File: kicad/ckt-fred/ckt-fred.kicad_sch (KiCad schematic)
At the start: 20 parts, among them J2 AVR-ISP, U1 AP7381-33Y

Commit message: Start of FRED PCB
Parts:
- BT1: renamed from BT?; footprint (none) -> Battery:BatteryHolder_Keystone_3034_1x20mm
- D5: renamed from D?; value CDBM140G -> BAT43W
- R1, R2: renamed from R?; footprint (none) -> Resistor_SMD:R_0805_2012Metric
- gave numbers to parts that had none: 5
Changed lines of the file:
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@@
   (symbol (lib_id "Device:R_US") (at 132.08 119.38 90) (unit 1)
     (in_bom yes) (on_board yes) (fields_autoplaced)
-    (property "Reference" "R?" (id 0) (at 132.08 113.03 90))
+    (property "Reference" "R2" (id 0) (at 132.08 113.03 90))
     (property "Value" "330" (id 1) (at 132.08 115.57 90))
-    (property "Footprint" "" (id 2) (at 132.334 118.364 90)
+    (property "Footprint" "Resistor_SMD:R_0805_2012Metric" (id 2) (at 132.334 118.364 90)
       (effects (font (size 1.27 1.27)) hide)
     )
@@
   (symbol (lib_id "MCU_Microchip_ATtiny:ATtiny13-20SS") (at 117.475 89.535 0) (mirror y) (unit 1)
     (in_bom yes) (on_board yes) (fields_autoplaced)
-    (property "Reference" "U?" (id 0) (at 131.445 88.2649 0)
-      (effects (font (size 1.27 1.27)) (justify right))
-    )
-    (property "Value" "ATtiny13-20SS" (id 1) (at 131.445 90.8049 0)
+    (property "Reference" "U3" (id 0) (at 132.08 88.2649 0)
+      (effects (font (size 1.27 1.27)) (justify right))
+    )
+    (property "Value" "ATtiny13-20SS" (id 1) (at 132.08 90.8049 0)
       (effects (font (size 1.27 1.27)) (justify right))
     )
@@
   (symbol (lib_id "power:GND") (at 144.78 125.095 0) (unit 1)
     (in_bom yes) (on_board yes)
-    (property "Reference" "#PWR?" (id 0) (at 144.78 131.445 0)
+    (property "Reference" "#PWR06" (id 0) (at 144.78 131.445 0)
       (effects (font (size 1.27 1.27)) hide)
     )
@@
   (symbol (lib_id "power:GND") (at 97.79 111.125 0) (unit 1)
     (in_bom yes) (on_board yes)
-    (property "Reference" "#PWR?" (id 0) (at 97.79 117.475 0)
+    (property "Reference" "#PWR02" (id 0) (at 97.79 117.475 0)
       (effects (font (size 1.27 1.27)) hide)
     )
@@
   (symbol (lib_id "Device:D_Schottky") (at 128.905 28.575 0) (mirror x) (unit 1)
     (in_bom yes) (on_board yes)
-    (property "Reference" "D?" (id 0) (at 132.08 31.115 0)
-      (effects (font (size 1.27 1.27)) (justify right))
-    )
-    (property "Value" "CDBM140G" (id 1) (at 127.635 31.115 0)
-      (effects (font (size 1.27 1.27)) (justify right) hide)
+    (property "Reference" "D5" (id 0) (at 132.08 31.115 0)
+      (effects (font (size 1.27 1.27)) (justify right))
+    )
+    (property "Value" "BAT43W" (id 1) (at 127.635 31.115 0)
+      (effects (font (size 1.27 1.27)) (justify right))
     )
     (property "Footprint" "ISE_Generic:SOD-123T" (id 2) (at 128.905 28.575 0)
@@
   (symbol (lib_id "Connector:TestPoint") (at 149.86 121.92 270) (mirror x) (unit 1)
     (in_bom yes) (on_board yes)
-    (property "Reference" "TP?" (id 0) (at 152.4 124.46 90)
+    (property "Reference" "TP3" (id 0) (at 152.4 124.46 90)
       (effects (font (size 1.27 1.27)) (justify right))
     )
@@
   (symbol (lib_id "Jumper:SolderJumper_2_Open") (at 97.79 107.315 90) (unit 1)
     (in_bom yes) (on_board yes)
-    (property "Reference" "JP?" (id 0) (at 95.25 107.315 0))
+    (property "Reference" "JP1" (id 0) (at 95.25 107.315 0))
     (property "Value" "SolderJumper_2_Open" (id 1) (at 95.25 107.315 0)
       (effects (font (size 1.27 1.27)) hide)
@@
   (symbol (lib_id "Device:R_US") (at 52.705 97.155 0) (unit 1)
     (in_bom yes) (on_board yes) (fields_autoplaced)
-    (property "Reference" "R?" (id 0) (at 54.61 95.8849 0)
+    (property "Reference" "R1" (id 0) (at 54.61 95.8849 0)
       (effects (font (size 1.27 1.27)) (justify left))
     )
@@
       (effects (font (size 1.27 1.27)) (justify left))
     )
-    (property "Footprint" "" (id 2) (at 53.721 97.409 90)
+    (property "Footprint" "Resistor_SMD:R_0805_2012Metric" (id 2) (at 53.721 97.409 90)
       (effects (font (size 1.27 1.27)) hide)
     )
@@
   (symbol (lib_id "Device:Battery_Cell") (at 137.795 36.83 0) (unit 1)
     (in_bom yes) (on_board yes) (fields_autoplaced)
-    (property "Reference" "BT?" (id 0) (at 140.97 33.5279 0)
+    (property "Reference" "BT1" (id 0) (at 140.97 33.5279 0)
       (effects (font (size 1.27 1.27)) (justify left))
     )
@@
       (effects (font (size 1.27 1.27)) (justify left))
     )
-    (property "Footprint" "" (id 2) (at 137.795 35.306 90)
+    (property "Footprint" "Battery:BatteryHolder_Keystone_3034_1x20mm" (id 2) (at 137.795 35.306 90)
       (effects (font (size 1.27 1.27)) hide)
     )
@@
   (symbol (lib_id "power:GND") (at 36.83 114.3 0) (unit 1)
     (in_bom yes) (on_board yes)
-    (property "Reference" "#PWR?" (id 0) (at 36.83 120.65 0)
+    (property "Reference" "#PWR03" (id 0) (at 36.83 120.65 0)
       (effects (font (size 1.27 1.27)) hide)
     )
@@
   (symbol (lib_id "Connector:TestPoint") (at 149.86 119.38 270) (mirror x) (unit 1)
     (in_bom yes) (on_board yes)
-    (property "Reference" "TP?" (id 0) (at 148.59 117.475 90)
+    (property "Reference" "TP4" (id 0) (at 148.59 117.475 90)
       (effects (font (size 1.27 1.27)) (justify left))
     )
@@
   (symbol (lib_id "power:+3.3V") (at 36.83 86.995 0) (unit 1)
     (in_bom yes) (on_board yes)
-    (property "Reference" "#PWR?" (id 0) (at 36.83 90.805 0)
+    (property "Reference" "#PWR01" (id 0) (at 36.83 90.805 0)
       (effects (font (size 1.27 1.27)) hide)
     )
@@
   (symbol (lib_id "Sensor_Magnetic:DRV5033AJxDBZ") (at 39.37 104.14 0) (unit 1)
     (in_bom yes) (on_board yes) (fields_autoplaced)
-    (property "Reference" "U?" (id 0) (at 33.02 102.8699 0)
+    (property "Reference" "U2" (id 0) (at 33.02 102.8699 0)
       (effects (font (size 1.27 1.27)) (justify right))
     )
@@
   )
   (symbol_instances
+    (path "/c35f82c3-3c27-45b4-98d2-54a981722db7"
+      (reference "#PWR01") (unit 1) (value "+3.3V") (footprint "")
+    )
+    (path "/42964190-2646-44c8-8c9c-8b8e84134411"
+      (reference "#PWR02") (unit 1) (value "GND") (footprint "")
+    )
+    (path "/b6f1eb09-ad2b-486b-b398-9172b42670fe"
+      (reference "#PWR03") (unit 1) (value "GND") (footprint "")
+    )
     (path "/ca6a6475-1ce9-4d3a-92ad-0b7481036c88"
       (reference "#PWR04") (unit 1) (value "+3.3V") (footprint "")
@@
       (reference "#PWR05") (unit 1) (value "GND") (footprint "")
     )
+    (path "/14cc276f-9bde-461b-a8e9-cda296e71d13"
+      (reference "#PWR06") (unit 1) (value "GND") (footprint "")
+    )
     (path "/2a960e4c-7bd7-45a1-abd2-4f9380b618df"
       (reference "#PWR0105") (unit 1) (value "GND") (footprint "")
@@
       (reference "#PWR0113") (unit 1) (value "GND") (footprint "")
     )
-    (path "/14cc276f-9bde-461b-a8e9-cda296e71d13"
-      (reference "#PWR?") (unit 1) (value "GND") (footprint "")
-    )
-    (path "/42964190-2646-44c8-8c9c-8b8e84134411"
-      (reference "#PWR?") (unit 1) (value "GND") (footprint "")
-    )
-    (path "/b6f1eb09-ad2b-486b-b398-9172b42670fe"
-      (reference "#PWR?") (unit 1) (value "GND") (footprint "")
-    )
-    (path "/c35f82c3-3c27-45b4-98d2-54a981722db7"
-      (reference "#PWR?") (unit 1) (value "+3.3V") (footprint "")
-    )
     (path "/9a1452f2-4147-4a0f-b89d-767540ba8421"
-      (reference "BT?") (unit 1) (value "Battery_Cell") (footprint "")
+      (reference "BT1") (unit 1) (value "Battery_Cell") (footprint "Battery:BatteryHolder_Keystone_3034_1x20mm")
     )
     (path "/469e5709-28b1-4cf7-9f12-16395fc286c3"
@@
     )
     (path "/42bb5574-8de7-4a27-a12d-7306121c342e"
-      (reference "D?") (unit 1) (value "CDBM140G") (footprint "ISE_Generic:SOD-123T")
+      (reference "D5") (unit 1) (value "BAT43W") (footprint "ISE_Generic:SOD-123T")
     )
     (path "/743fd467-fa48-43d2-bdb1-0e709d925207"
@@
     )
     (path "/63977e5d-25ea-40a1-a869-d864a691de83"
-      (reference "JP?") (unit 1) (value "SolderJumper_2_Open") (footprint "Jumper:SolderJumper-2_P1.3mm_Open_RoundedPad1.0x1.5mm")
+      (reference "JP1") (unit 1) (value "SolderJumper_2_Open") (footprint "Jumper:SolderJumper-2_P1.3mm_Open_RoundedPad1.0x1.5mm")
+    )
+    (path "/8219c475-d6a1-455a-8dd4-ef0923356e4f"
+      (reference "R1") (unit 1) (value "100k") (footprint "Resistor_SMD:R_0805_2012Metric")
     )
     (path "/0aee1d11-4153-4a66-aa82-53a758d11c70"
-      (reference "R?") (unit 1) (value "330") (footprint "")
-    )
-    (path "/8219c475-d6a1-455a-8dd4-ef0923356e4f"
-      (reference "R?") (unit 1) (value "100k") (footprint "")
+      (reference "R2") (unit 1) (value "330") (footprint "Resistor_SMD:R_0805_2012Metric")
     )
     (path "/3d36f4c8-bdba-4d9c-8bb5-9b4a29689543"
@@
     )
     (path "/611c3ee3-155a-43e9-93d8-4698eb221164"
-      (reference "TP?") (unit 1) (value "TestPoint") (footprint "TestPoint:TestPoint_Pad_D2.0mm")
+      (reference "TP3") (unit 1) (value "TestPoint") (footprint "TestPoint:TestPoint_Pad_D2.0mm")
     )
     (path "/be05cc19-b0f7-4496-b019-4138adf19a10"
-      (reference "TP?") (unit 1) (value "TestPoint") (footprint "TestPoint:TestPoint_Pad_D2.0mm")
+      (reference "TP4") (unit 1) (value "TestPoint") (footprint "TestPoint:TestPoint_Pad_D2.0mm")
     )
     (path "/7a02355a-c87d-4d7e-9caa-076f50357812"
       (reference "U1") (unit 1) (value "AP7381-33Y") (footprint "ISE_Generic:SOT-89-3")
     )
+    (path "/d6778ce1-2501-4a7c-a126-0ea376c756f4"
+      (reference "U2") (unit 1) (value "DRV5032") (footprint "Package_TO_SOT_SMD:SOT-23")
+    )
     (path "/0cc7314a-3dbf-4203-939f-6c8913def138"
-      (reference "U?") (unit 1) (value "ATtiny13-20SS") (footprint "Package_SO:SOIC-8_3.9x4.9mm_P1.27mm")
-    )
-    (path "/d6778ce1-2501-4a7c-a126-0ea376c756f4"
-      (reference "U?") (unit 1) (value "DRV5032") (footprint "Package_TO_SOT_SMD:SOT-23")
-    )
-  )
+      (reference "U3") (unit 1) (value "ATtiny13-20SS") (footprint "Package_SO:SOIC-8_3.9x4.9mm_P1.27mm")
+    )
+  )

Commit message: A few updates
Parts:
- TP1, TP2, TP3, TP4: footprint TestPoint:TestPoint_Pad_D2.0mm -> TestPoint:TestPoint_Pad_4.0x4.0mm
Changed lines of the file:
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@@
       (effects (font (size 1.27 1.27)) (justify left) hide)
     )
-    (property "Footprint" "TestPoint:TestPoint_Pad_D2.0mm" (id 2) (at 29.21 23.495 0)
+    (property "Footprint" "TestPoint:TestPoint_Pad_4.0x4.0mm" (id 2) (at 29.21 23.495 0)
       (effects (font (size 1.27 1.27)) hide)
     )
@@
       (effects (font (size 1.27 1.27)) (justify left) hide)
     )
-    (property "Footprint" "TestPoint:TestPoint_Pad_D2.0mm" (id 2) (at 149.86 116.84 0)
+    (property "Footprint" "TestPoint:TestPoint_Pad_4.0x4.0mm" (id 2) (at 149.86 116.84 0)
       (effects (font (size 1.27 1.27)) hide)
     )
@@
       (effects (font (size 1.27 1.27)) (justify left) hide)
     )
-    (property "Footprint" "TestPoint:TestPoint_Pad_D2.0mm" (id 2) (at 29.21 26.035 0)
+    (property "Footprint" "TestPoint:TestPoint_Pad_4.0x4.0mm" (id 2) (at 29.21 26.035 0)
       (effects (font (size 1.27 1.27)) hide)
     )
@@
       (effects (font (size 1.27 1.27)) (justify left) hide)
     )
-    (property "Footprint" "TestPoint:TestPoint_Pad_D2.0mm" (id 2) (at 149.86 114.3 0)
+    (property "Footprint" "TestPoint:TestPoint_Pad_4.0x4.0mm" (id 2) (at 149.86 114.3 0)
       (effects (font (size 1.27 1.27)) hide)
     )
@@
     )
     (path "/3d36f4c8-bdba-4d9c-8bb5-9b4a29689543"
-      (reference "TP1") (unit 1) (value "TestPoint") (footprint "TestPoint:TestPoint_Pad_D2.0mm")
+      (reference "TP1") (unit 1) (value "TestPoint") (footprint "TestPoint:TestPoint_Pad_4.0x4.0mm")
     )
     (path "/6e81bcf9-ab29-4e46-90b9-1f0815b829a0"
-      (reference "TP2") (unit 1) (value "TestPoint") (footprint "TestPoint:TestPoint_Pad_D2.0mm")
+      (reference "TP2") (unit 1) (value "TestPoint") (footprint "TestPoint:TestPoint_Pad_4.0x4.0mm")
     )
     (path "/611c3ee3-155a-43e9-93d8-4698eb221164"
-      (reference "TP3") (unit 1) (value "TestPoint") (footprint "TestPoint:TestPoint_Pad_D2.0mm")
+      (reference "TP3") (unit 1) (value "TestPoint") (footprint "TestPoint:TestPoint_Pad_4.0x4.0mm")
     )
     (path "/be05cc19-b0f7-4496-b019-4138adf19a10"
-      (reference "TP4") (unit 1) (value "TestPoint") (footprint "TestPoint:TestPoint_Pad_D2.0mm")
+      (reference "TP4") (unit 1) (value "TestPoint") (footprint "TestPoint:TestPoint_Pad_4.0x4.0mm")
     )
     (path "/7a02355a-c87d-4d7e-9caa-076f50357812"

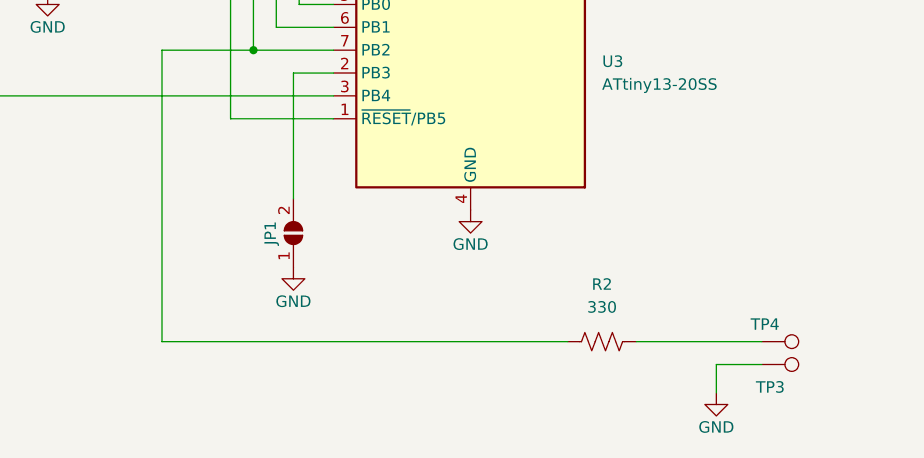
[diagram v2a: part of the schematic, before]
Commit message: Add output jumper to bypass resistor
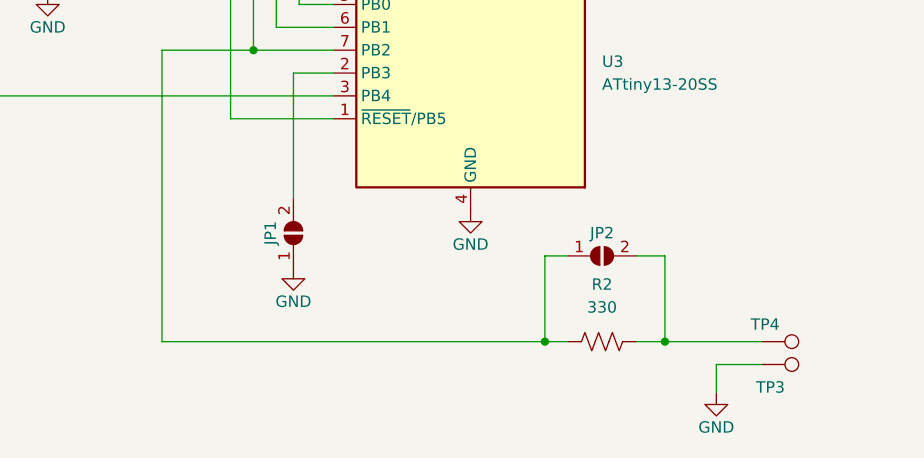
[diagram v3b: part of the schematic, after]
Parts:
- added JP2: SolderJumper_2_Open, Jumper:SolderJumper-2_P1.3mm_Open_RoundedPad1.0x1.5mm, symbol Jumper:SolderJumper_2_Open
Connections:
- net at J2.3 (SCK), R2.1, U3.7 (PB2): now also JP2.1 (A)
- net at R2.2, TP4.1: now also JP2.2 (B)
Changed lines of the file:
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@@
   (junction (at 69.215 46.355) (diameter 0) (color 0 0 0 0)
   )
+  (junction (at 139.065 119.38) (diameter 0) (color 0 0 0 0)
+  )
   (junction (at 118.11 28.575) (diameter 0) (color 0 0 0 0)
   )
   (junction (at 102.235 46.355) (diameter 0) (color 0 0 0 0)
   )
+  (junction (at 125.73 119.38) (diameter 0) (color 0 0 0 0)
+  )
   (junction (at 102.235 28.575) (diameter 0) (color 0 0 0 0)
   )
@@
     (stroke (width 0) (type default) (color 0 0 0 0))
   )
-  (wire (pts (xy 135.89 119.38) (xy 149.86 119.38))
+  (wire (pts (xy 135.89 119.38) (xy 139.065 119.38))
+    (stroke (width 0) (type default) (color 0 0 0 0))
+  )
+  (wire (pts (xy 125.73 119.38) (xy 83.185 119.38))
     (stroke (width 0) (type default) (color 0 0 0 0))
   )
@@
     (stroke (width 0) (type default) (color 0 0 0 0))
   )
+  (wire (pts (xy 139.065 109.855) (xy 139.065 119.38))
+    (stroke (width 0) (type default) (color 0 0 0 0))
+  )
   (wire (pts (xy 144.78 121.92) (xy 149.86 121.92))
     (stroke (width 0) (type default) (color 0 0 0 0))
@@
     (stroke (width 0) (type default) (color 0 0 0 0))
   )
+  (wire (pts (xy 135.89 109.855) (xy 139.065 109.855))
+    (stroke (width 0) (type default) (color 0 0 0 0))
+  )
   (wire (pts (xy 29.21 31.115) (xy 42.037 31.115))
     (stroke (width 0) (type default) (color 0 0 0 0))
@@
     (stroke (width 0) (type default) (color 0 0 0 0))
   )
+  (wire (pts (xy 128.27 109.855) (xy 125.73 109.855))
+    (stroke (width 0) (type default) (color 0 0 0 0))
+  )
   (wire (pts (xy 95.885 73.025) (xy 95.885 84.455))
     (stroke (width 0) (type default) (color 0 0 0 0))
@@
     (stroke (width 0) (type default) (color 0 0 0 0))
   )
+  (wire (pts (xy 125.73 109.855) (xy 125.73 119.38))
+    (stroke (width 0) (type default) (color 0 0 0 0))
+  )
   (wire (pts (xy 102.235 92.075) (xy 59.69 92.075))
     (stroke (width 0) (type default) (color 0 0 0 0))
@@
     (stroke (width 0) (type default) (color 0 0 0 0))
   )
+  (wire (pts (xy 139.065 119.38) (xy 149.86 119.38))
+    (stroke (width 0) (type default) (color 0 0 0 0))
+  )
   (wire (pts (xy 102.235 46.355) (xy 118.11 46.355))
     (stroke (width 0) (type default) (color 0 0 0 0))
@@
     (stroke (width 0) (type default) (color 0 0 0 0))
   )
-  (wire (pts (xy 128.27 119.38) (xy 83.185 119.38))
+  (wire (pts (xy 128.27 119.38) (xy 125.73 119.38))
     (stroke (width 0) (type default) (color 0 0 0 0))
   )
@@
     (pin "3")
   )
+  (symbol (lib_id "Jumper:SolderJumper_2_Open") (at 132.08 109.855 0) (unit 1)
+    (in_bom yes) (on_board yes)
+    (property "Reference" "JP2" (id 0) (at 132.08 107.315 0))
+    (property "Value" "SolderJumper_2_Open" (id 1) (at 132.08 107.315 0)
+      (effects (font (size 1.27 1.27)) hide)
+    )
+    (property "Footprint" "Jumper:SolderJumper-2_P1.3mm_Open_RoundedPad1.0x1.5mm" (id 2) (at 132.08 109.855 0)
+      (effects (font (size 1.27 1.27)) hide)
+    )
+    (property "Datasheet" "~" (id 3) (at 132.08 109.855 0)
+      (effects (font (size 1.27 1.27)) hide)
+    )
+    (pin "1")
+    (pin "2")
+  )
   (symbol (lib_id "Device:R_US") (at 52.705 97.155 0) (unit 1)
     (in_bom yes) (on_board yes) (fields_autoplaced)
@@
       (reference "JP1") (unit 1) (value "SolderJumper_2_Open") (footprint "Jumper:SolderJumper-2_P1.3mm_Open_RoundedPad1.0x1.5mm")
     )
+    (path "/7fc6b1a5-c57c-409f-b3f1-6370c6e30921"
+      (reference "JP2") (unit 1) (value "SolderJumper_2_Open") (footprint "Jumper:SolderJumper-2_P1.3mm_Open_RoundedPad1.0x1.5mm")
+    )
     (path "/8219c475-d6a1-455a-8dd4-ef0923356e4f"
